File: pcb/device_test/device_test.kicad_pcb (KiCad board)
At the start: 4 copper layers, 80 x 80 mm, 24 parts, among them J101 Screw_Terminal_01x02, J201 USB_C_Receptacle_USB2.0_16P, J202 Conn_01x04, J203 Conn_02x10_Row_Letter_First, J301 USB_C_Receptacle_USB2.0_16P, J302 Conn_02x10_Row_Letter_First

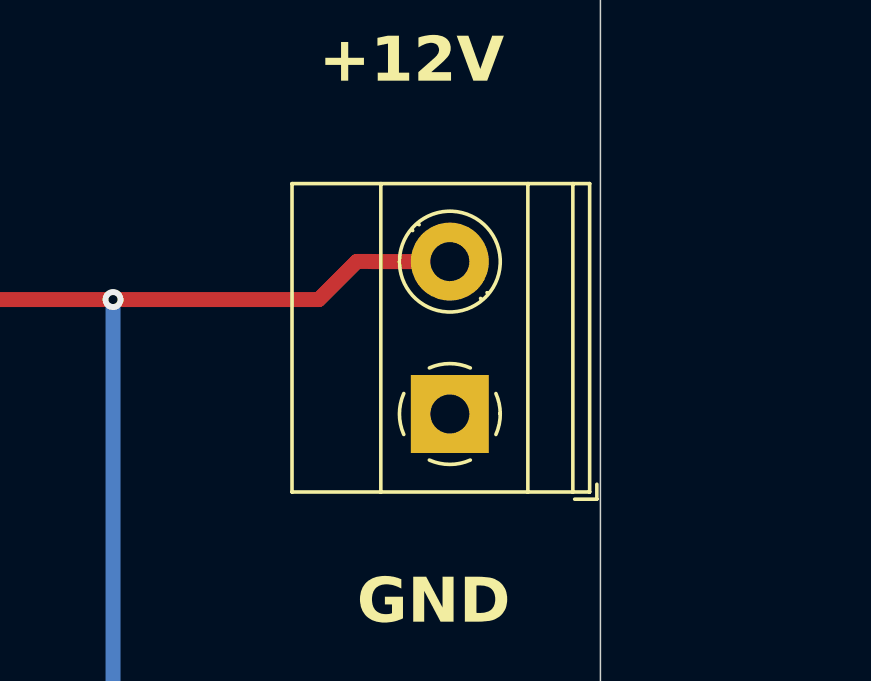
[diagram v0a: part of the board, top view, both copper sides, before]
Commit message: upgrade to kicad 9.0.0
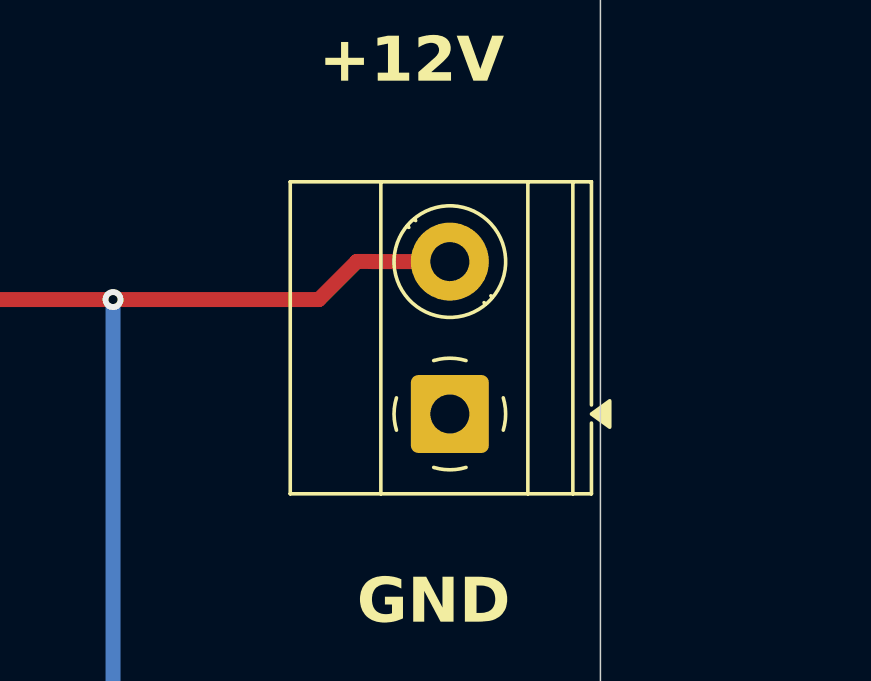
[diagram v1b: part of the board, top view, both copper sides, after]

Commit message: fixes
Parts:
- moved C301 67.0 mm to (102.9, 98.6), turned to -90 degrees
- moved #SYM101 52.0 mm to (100.5, 58.6)
- moved C201 42.8 mm to (132.3, 63.3)
- moved REF** 41.6 mm to (85.2, 46.6)
- moved J302 37.4 mm to (86.6, 103.0)
- moved REF** 35.6 mm to (85.2, 136.6)
- moved J203 33.5 mm to (118.8, 46.8)
- moved J202 33.5 mm to (118.7, 58.6)
- moved C101 28.8 mm to (141.7, 72.3)
- moved REF** 26.7 mm to (175.2, 46.6)
- moved R201 25.6 mm to (126.8, 129.6)
- moved R202 25.6 mm to (133.9, 129.6)
- moved J201 25.6 mm to (130.3, 137.8)
- moved R303 21.6 mm to (152.1, 117.5)
- moved D201 21.6 mm to (156.7, 114.0)
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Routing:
- net +12V: track 181.4 -> 216.0 mm
- net +5V_A: track 119.6 -> 150.7 mm, vias 3 -> 1
- net +5V_B: track 109.1 -> 136.3 mm
- net /Device Tester Connector/USB-: track 70.7 -> 91.6 mm
- net /Device Tester Connector/USB+: track 71.6 -> 91.7 mm
- net /Bus Tester Connector/USB-: track 69.7 -> 89.7 mm
- net /Bus Tester Connector/USB+: track 69.8 -> 89.8 mm
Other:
- board size 80 x 80 mm -> 100 x 100 mm

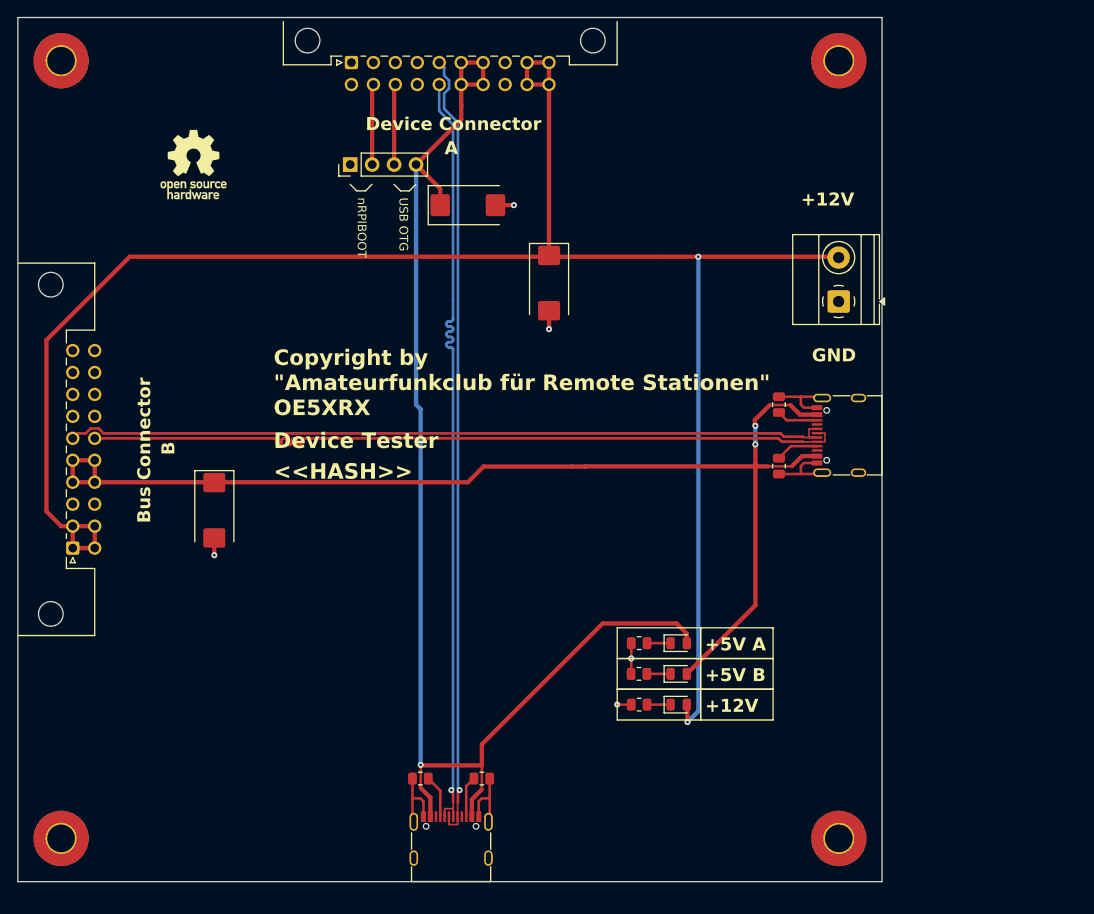
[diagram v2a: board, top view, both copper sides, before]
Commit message: change mounting hole
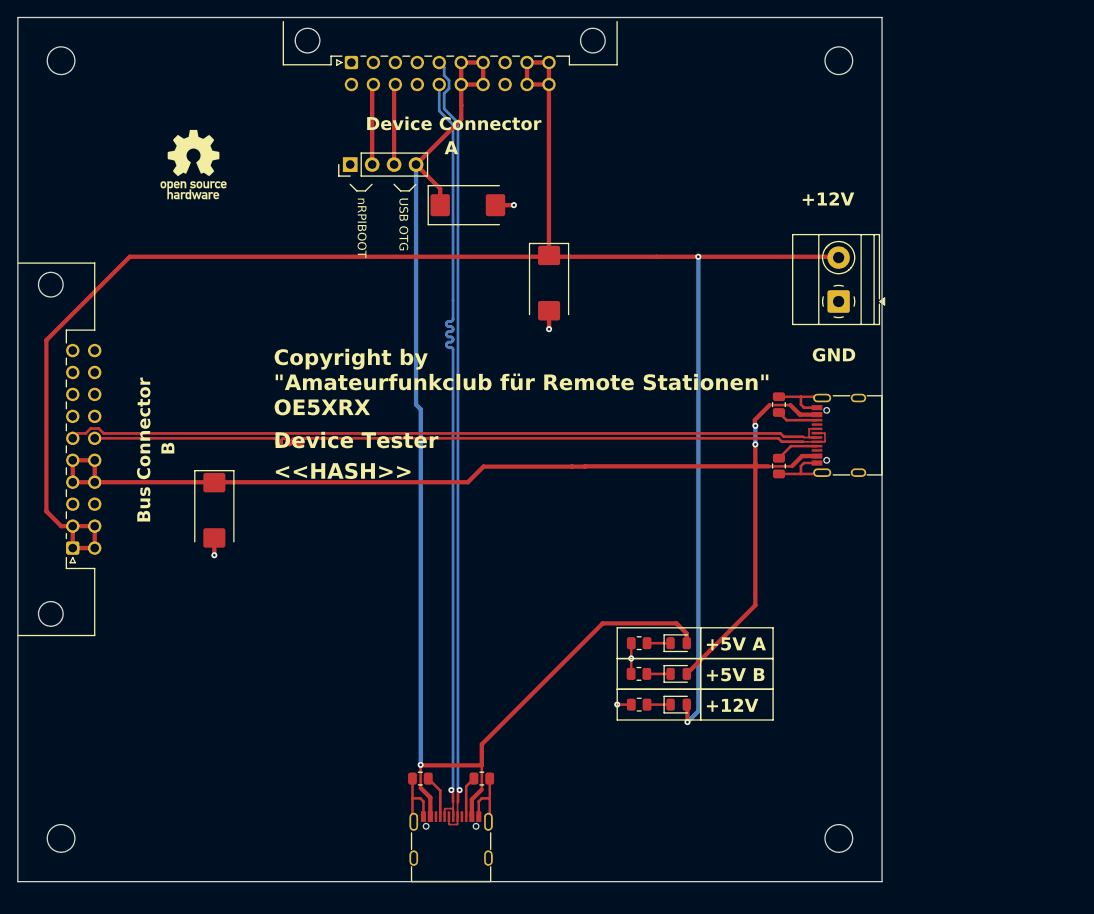
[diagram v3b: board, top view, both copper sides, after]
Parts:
- H101, H102, H103, H104: renamed from REF**; value MountingHole_3.2mm_M3_Pad_TopBottom -> MountingHole; footprint MountingHole:MountingHole_3.2mm_M3_Pad_TopBottom -> MountingHole:MountingHole_3.2mm_M3
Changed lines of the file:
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@@
 	(net 30 "unconnected-(J302-Pin_a9-Pada9)")
 	(net 31 "unconnected-(J302-Pin_b8-Padb8)")
-	(footprint "MountingHole:MountingHole_3.2mm_M3_Pad_TopBottom"
+	(footprint "MountingHole:MountingHole_3.2mm_M3"
 		(layer "F.Cu")
 		(at 85.204 46.562)
-		(descr "Mounting Hole 3.2mm, M3")
-		(tags "mounting hole 3.2mm m3")
-		(property "Reference" "REF**"
+		(descr "Mounting Hole 3.2mm, no annular, M3")
+		(tags "mounting hole 3.2mm no annular m3")
+		(property "Reference" "H101"
 			(at 0 -4.2 0)
 			(layer "F.SilkS")
@@
 			)
 		)
-		(property "Value" "MountingHole_3.2mm_M3_Pad_TopBottom"
+		(property "Value" "MountingHole"
 			(at 0 4.2 0)
 			(layer "F.Fab")
@@
 			)
 		)
-		(property "Description" ""
+		(property "Description" "Mounting Hole without connection"
 			(at 0 0 0)
 			(unlocked yes)
@@
 			)
 		)
-		(attr board_only exclude_from_pos_files exclude_from_bom)
+		(property "LCSC" ""
+			(at 0 0 0)
+			(unlocked yes)
+			(layer "F.Fab")
+			(hide yes)
+			(effects
+				(font
+					(size 1 1)
+					(thickness 0.15)
+				)
+			)
+		)
+		(property ki_fp_filters "MountingHole*")
+		(sheetname "/")
+		(sheetfile "device_test.kicad_sch")
+		(attr exclude_from_pos_files exclude_from_bom)
 		(fp_circle
 			(center 0 0)
@@
 			)
 		)
-		(pad "1" thru_hole circle
+		(pad "" np_thru_hole circle
 			(at 0 0)
-			(size 3.6 3.6)
+			(size 3.2 3.2)
 			(drill 3.2)
 			(layers "*.Cu" "*.Mask")
-			(remove_unused_layers no)
-		)
-		(pad "1" connect circle
-			(at 0 0)
-			(size 6.4 6.4)
-			(layers "F.Cu" "F.Mask")
-		)
-		(pad "1" connect circle
-			(at 0 0)
-			(size 6.4 6.4)
-			(layers "B.Cu" "B.Mask")
 		)
 		(embedded_fonts no)
@@
 		)
 	)
-	(footprint "MountingHole:MountingHole_3.2mm_M3_Pad_TopBottom"
+	(footprint "MountingHole:MountingHole_3.2mm_M3"
 		(layer "F.Cu")
 		(at 175.204 136.562)
-		(descr "Mounting Hole 3.2mm, M3")
-		(tags "mounting hole 3.2mm m3")
-		(property "Reference" "REF**"
+		(descr "Mounting Hole 3.2mm, no annular, M3")
+		(tags "mounting hole 3.2mm no annular m3")
+		(property "Reference" "H104"
 			(at 0 -4.2 0)
 			(layer "F.SilkS")
@@
 			)
 		)
-		(property "Value" "MountingHole_3.2mm_M3_Pad_TopBottom"
+		(property "Value" "MountingHole"
 			(at 0 4.2 0)
 			(layer "F.Fab")
@@
 			)
 		)
-		(property "Description" ""
+		(property "Description" "Mounting Hole without connection"
 			(at 0 0 0)
 			(unlocked yes)
@@
 			)
 		)
-		(attr board_only exclude_from_pos_files exclude_from_bom)
+		(property "LCSC" ""
+			(at 0 0 0)
+			(unlocked yes)
+			(layer "F.Fab")
+			(hide yes)
+			(effects
+				(font
+					(size 1 1)
+					(thickness 0.15)
+				)
+			)
+		)
+		(property ki_fp_filters "MountingHole*")
+		(sheetname "/")
+		(sheetfile "device_test.kicad_sch")
+		(attr exclude_from_pos_files exclude_from_bom)
 		(fp_circle
 			(center 0 0)
@@
 			)
 		)
-		(pad "1" thru_hole circle
+		(pad "" np_thru_hole circle
 			(at 0 0)
-			(size 3.6 3.6)
+			(size 3.2 3.2)
 			(drill 3.2)
 			(layers "*.Cu" "*.Mask")
-			(remove_unused_layers no)
-		)
-		(pad "1" connect circle
-			(at 0 0)
-			(size 6.4 6.4)
-			(layers "F.Cu" "F.Mask")
-		)
-		(pad "1" connect circle
-			(at 0 0)
-			(size 6.4 6.4)
-			(layers "B.Cu" "B.Mask")
 		)
 		(embedded_fonts no)
@@
 		)
 	)
-	(footprint "MountingHole:MountingHole_3.2mm_M3_Pad_TopBottom"
+	(footprint "MountingHole:MountingHole_3.2mm_M3"
 		(layer "F.Cu")
 		(at 85.204 136.562)
-		(descr "Mounting Hole 3.2mm, M3")
-		(tags "mounting hole 3.2mm m3")
-		(property "Reference" "REF**"
+		(descr "Mounting Hole 3.2mm, no annular, M3")
+		(tags "mounting hole 3.2mm no annular m3")
+		(property "Reference" "H103"
 			(at 0 -4.2 0)
 			(layer "F.SilkS")
@@
 			)
 		)
-		(property "Value" "MountingHole_3.2mm_M3_Pad_TopBottom"
+		(property "Value" "MountingHole"
 			(at 0 4.2 0)
 			(layer "F.Fab")
@@
 			)
 		)
-		(property "Description" ""
+		(property "Description" "Mounting Hole without connection"
 			(at 0 0 0)
 			(unlocked yes)
@@
 			)
 		)
-		(attr board_only exclude_from_pos_files exclude_from_bom)
+		(property "LCSC" ""
+			(at 0 0 0)
+			(unlocked yes)
+			(layer "F.Fab")
+			(hide yes)
+			(effects
+				(font
+					(size 1 1)
+					(thickness 0.15)
+				)
+			)
+		)
+		(property ki_fp_filters "MountingHole*")
+		(sheetname "/")
+		(sheetfile "device_test.kicad_sch")
+		(attr exclude_from_pos_files exclude_from_bom)
 		(fp_circle
 			(center 0 0)
@@
 			)
 		)
-		(pad "1" thru_hole circle
+		(pad "" np_thru_hole circle
 			(at 0 0)
-			(size 3.6 3.6)
+			(size 3.2 3.2)
 			(drill 3.2)
 			(layers "*.Cu" "*.Mask")
-			(remove_unused_layers no)
-		)
-		(pad "1" connect circle
-			(at 0 0)
-			(size 6.4 6.4)
-			(layers "F.Cu" "F.Mask")
-		)
-		(pad "1" connect circle
-			(at 0 0)
-			(size 6.4 6.4)
-			(layers "B.Cu" "B.Mask")
 		)
 		(embedded_fonts no)
@@
 		)
 	)
-	(footprint "MountingHole:MountingHole_3.2mm_M3_Pad_TopBottom"
+	(footprint "MountingHole:MountingHole_3.2mm_M3"
 		(layer "F.Cu")
 		(at 175.204 46.562)
-		(descr "Mounting Hole 3.2mm, M3")
-		(tags "mounting hole 3.2mm m3")
-		(property "Reference" "REF**"
+		(descr "Mounting Hole 3.2mm, no annular, M3")
+		(tags "mounting hole 3.2mm no annular m3")
+		(property "Reference" "H102"
 			(at 0 -4.2 0)
 			(layer "F.SilkS")
@@
 			)
 		)
-		(property "Value" "MountingHole_3.2mm_M3_Pad_TopBottom"
+		(property "Value" "MountingHole"
 			(at 0 4.2 0)
 			(layer "F.Fab")
@@
 			)
 		)
-		(property "Description" ""
+		(property "Description" "Mounting Hole without connection"
 			(at 0 0 0)
 			(unlocked yes)
@@
 			)
 		)
-		(attr board_only exclude_from_pos_files exclude_from_bom)
+		(property "LCSC" ""
+			(at 0 0 0)
+			(unlocked yes)
+			(layer "F.Fab")
+			(hide yes)
+			(effects
+				(font
+					(size 1 1)
+					(thickness 0.15)
+				)
+			)
+		)
+		(property ki_fp_filters "MountingHole*")
+		(sheetname "/")
+		(sheetfile "device_test.kicad_sch")
+		(attr exclude_from_pos_files exclude_from_bom)
 		(fp_circle
 			(center 0 0)
@@
 			)
 		)
-		(pad "1" thru_hole circle
+		(pad "" np_thru_hole circle
 			(at 0 0)
-			(size 3.6 3.6)
+			(size 3.2 3.2)
 			(drill 3.2)
 			(layers "*.Cu" "*.Mask")
-			(remove_unused_layers no)
-		)
-		(pad "1" connect circle
-			(at 0 0)
-			(size 6.4 6.4)
-			(layers "F.Cu" "F.Mask")
-		)
-		(pad "1" connect circle
-			(at 0 0)
-			(size 6.4 6.4)
-			(layers "B.Cu" "B.Mask")
 		)
 		(embedded_fonts no)

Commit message: update ALL parts
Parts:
- C101, C201, C301: footprint Capacitor_Tantalum_SMD:CP_EIA-7343-43_Kemet-X_Pad2.25x2.55mm_HandSolder -> Capacitor_Tantalum_SMD:CP_EIA-7343-43_Kemet-X
- R203, R303: value 390 -> 1k

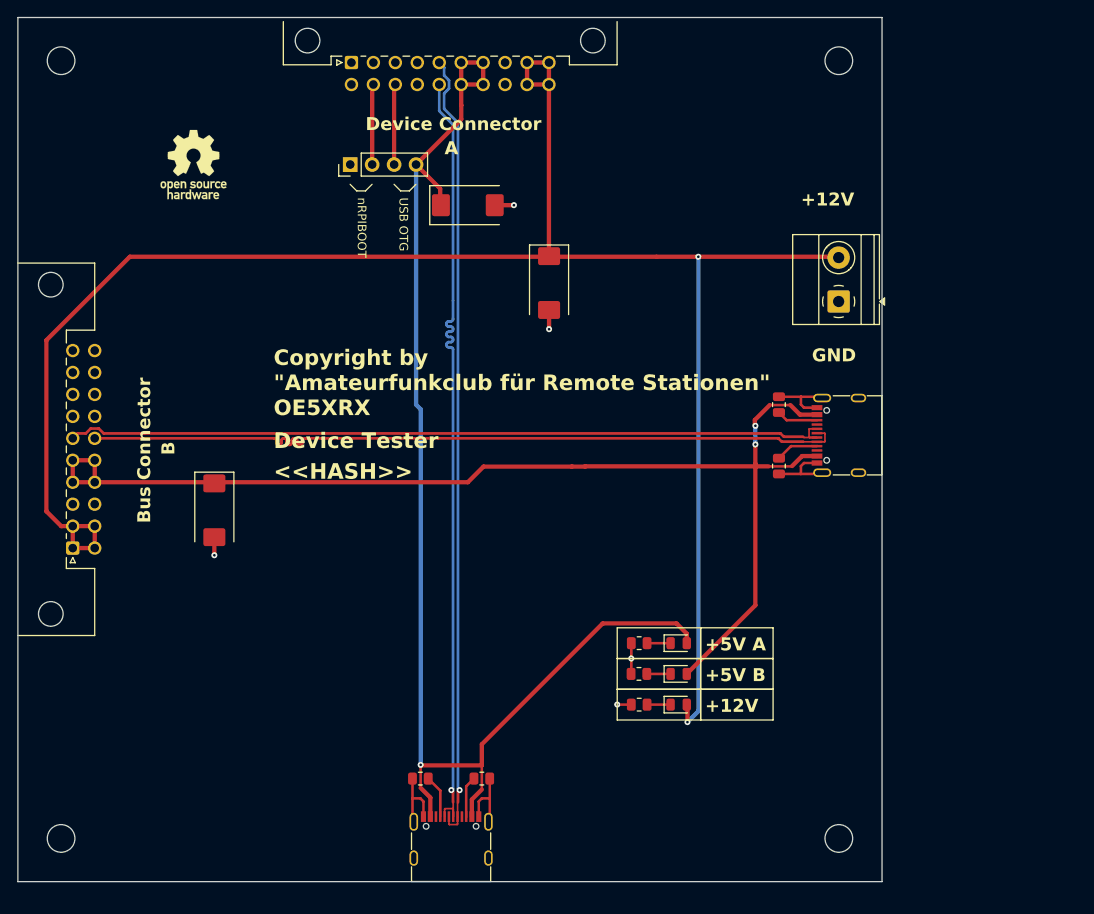
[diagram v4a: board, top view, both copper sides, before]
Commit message: fix device tester pcb
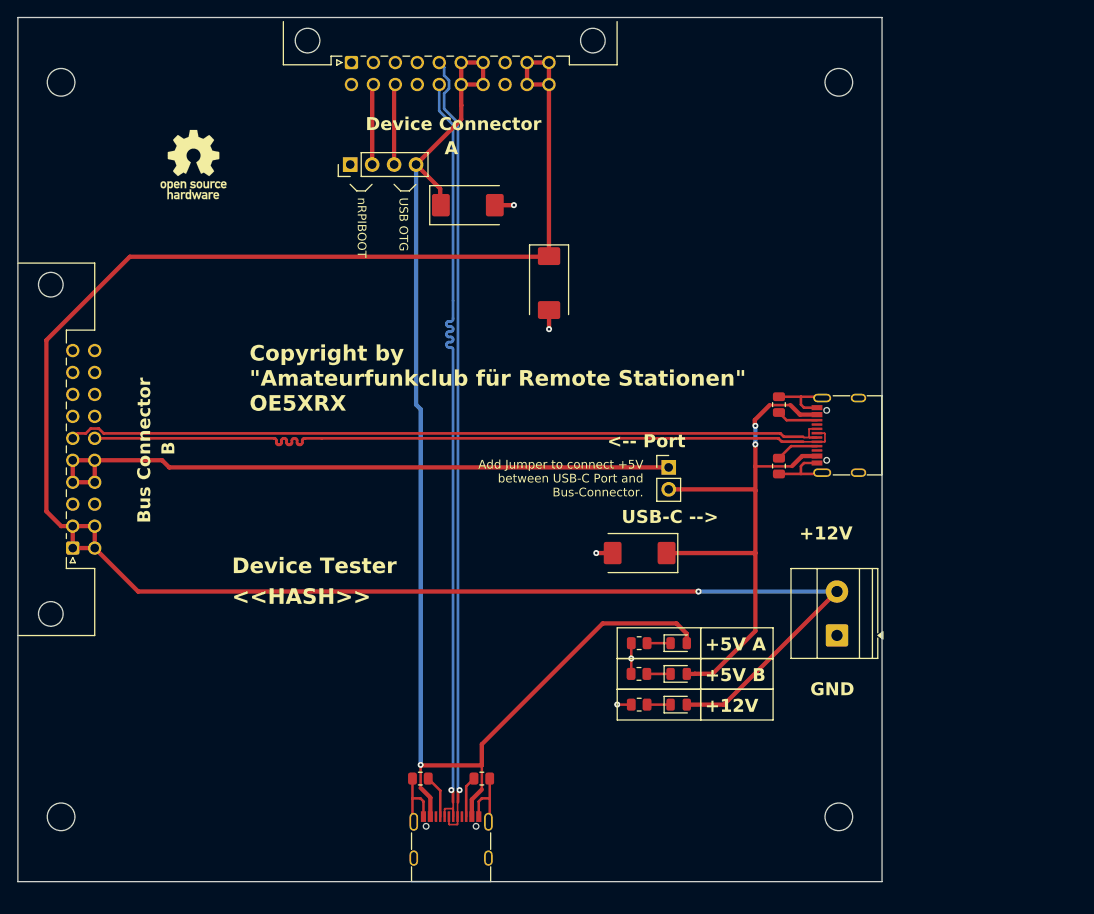
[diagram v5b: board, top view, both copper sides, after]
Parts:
- added J303: Conn_01x02_Pin, Connector_PinHeader_2.54mm:PinHeader_1x02_P2.54mm_Vertical, F.Cu at (155.5, 93.6)
- moved C301 49.5 mm to (152.2, 103.5), turned to 180 degrees
- moved J101 38.6 mm to (175.0, 113.1)
- moved H101 2.50 mm to (85.2, 49.1)
- moved H102 2.50 mm to (175.2, 49.1)
- moved H103 2.50 mm to (85.2, 134.1)
- moved H104 2.50 mm to (175.2, 134.1)
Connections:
- J302 pad a4: +5V_B -> Net-(J302-Pin_a4)
- J302 pad a5: +5V_B -> Net-(J302-Pin_a4)
- J302 pad b4: +5V_B -> Net-(J302-Pin_a4)
- J302 pad b5: +5V_B -> Net-(J302-Pin_a4)
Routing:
- net Net-(J302-Pin_a4): track 0.00 -> 76.9 mm
- net +5V_B: track 136.3 -> 70.8 mm
- net +12V: track 216.0 -> 237.1 mm, vias 2 -> 1
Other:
- board text added: "<-- Port"
- board text added: "Add Jumper to connect +5V between USB-C Port and Bus-Connector."
- board text added: "USB-C -->"
